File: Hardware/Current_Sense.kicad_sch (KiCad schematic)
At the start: 35 parts, among them IC2 INA241A4IDR, IC3 AMC1350DWVR, IC4 TLV9002QDRQ1, J6 Scrut Conn, SW3 Scrut Select, U9 REF35125QDBVR

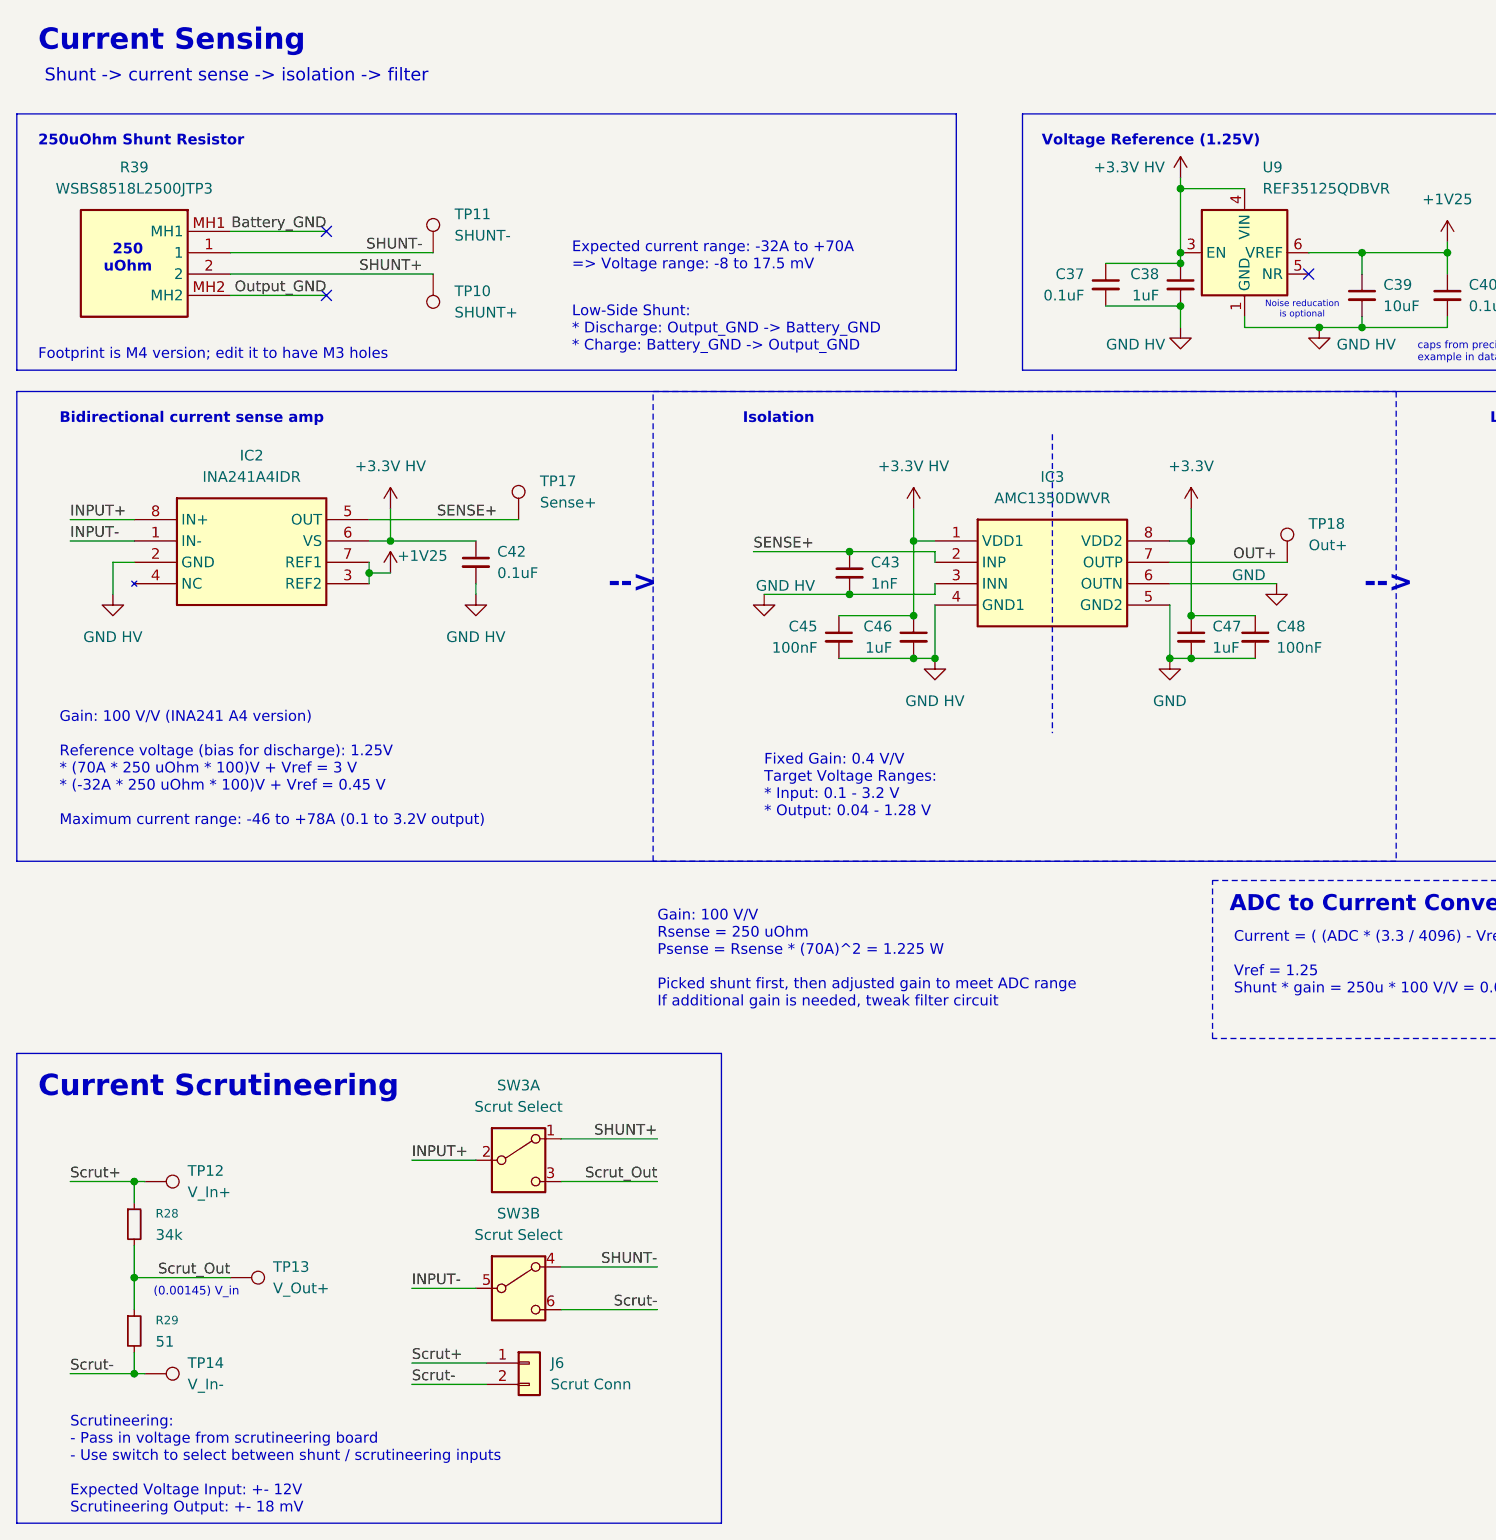
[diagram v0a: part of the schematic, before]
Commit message: added documentation for current range; added VBUS led
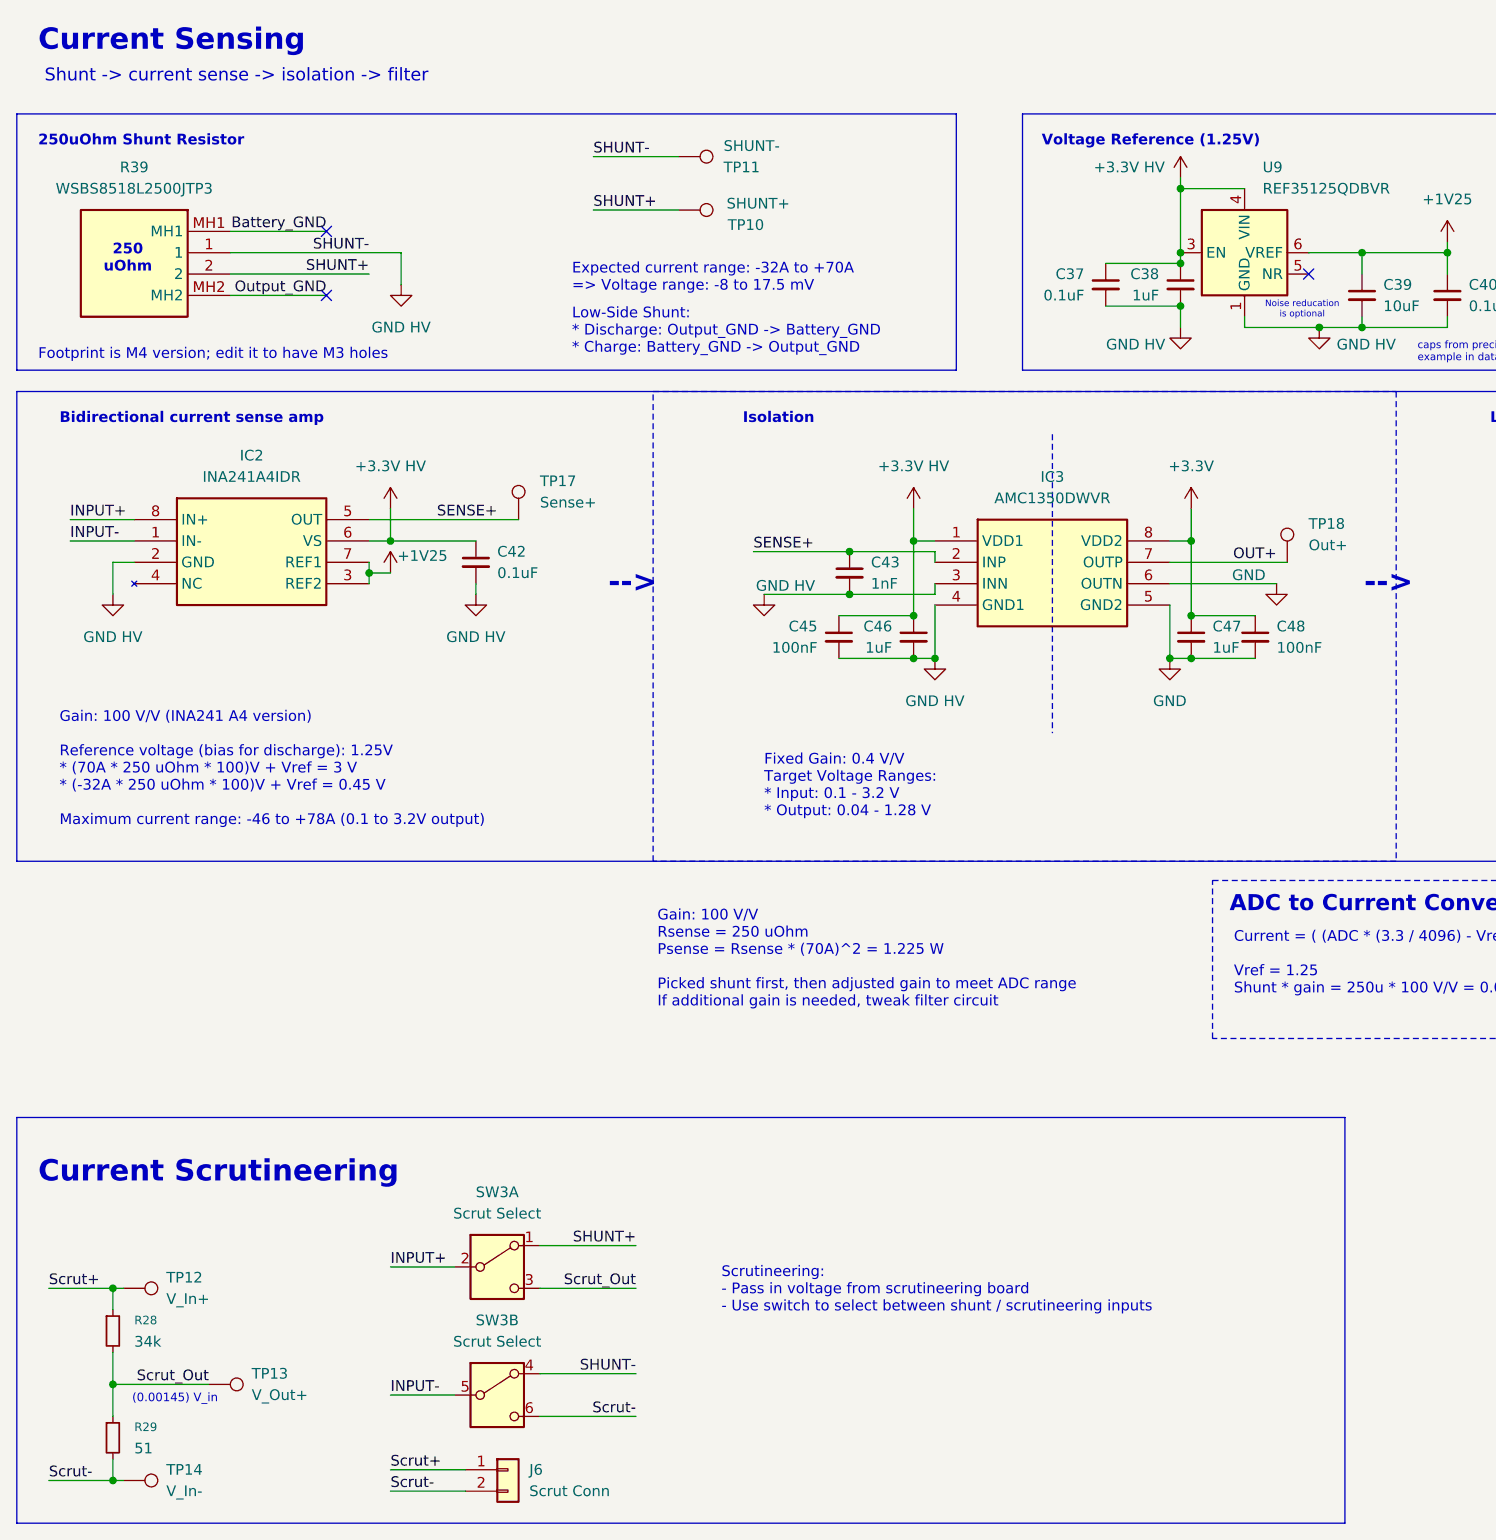
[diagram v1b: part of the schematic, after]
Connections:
- net SHUNT- is gone; now on net GND HV: R39.1, SW3.4 (A), TP11.1
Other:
- note added: "Scrutineering: - Pass in voltage from scrutineering board - Use switch to select between shunt / scrutineering inputs"
- note removed: "Scrutineering: - Pass in voltage from scrutineering board - Use switch to select between shunt / scrutineering inputs Expected Voltage Input: +- 12V Scrutineering Output: +- 18 mV"
- moved on the sheet: J6, R28, R29, SW3A, SW3B, TP10, TP11, TP12, TP13, TP14

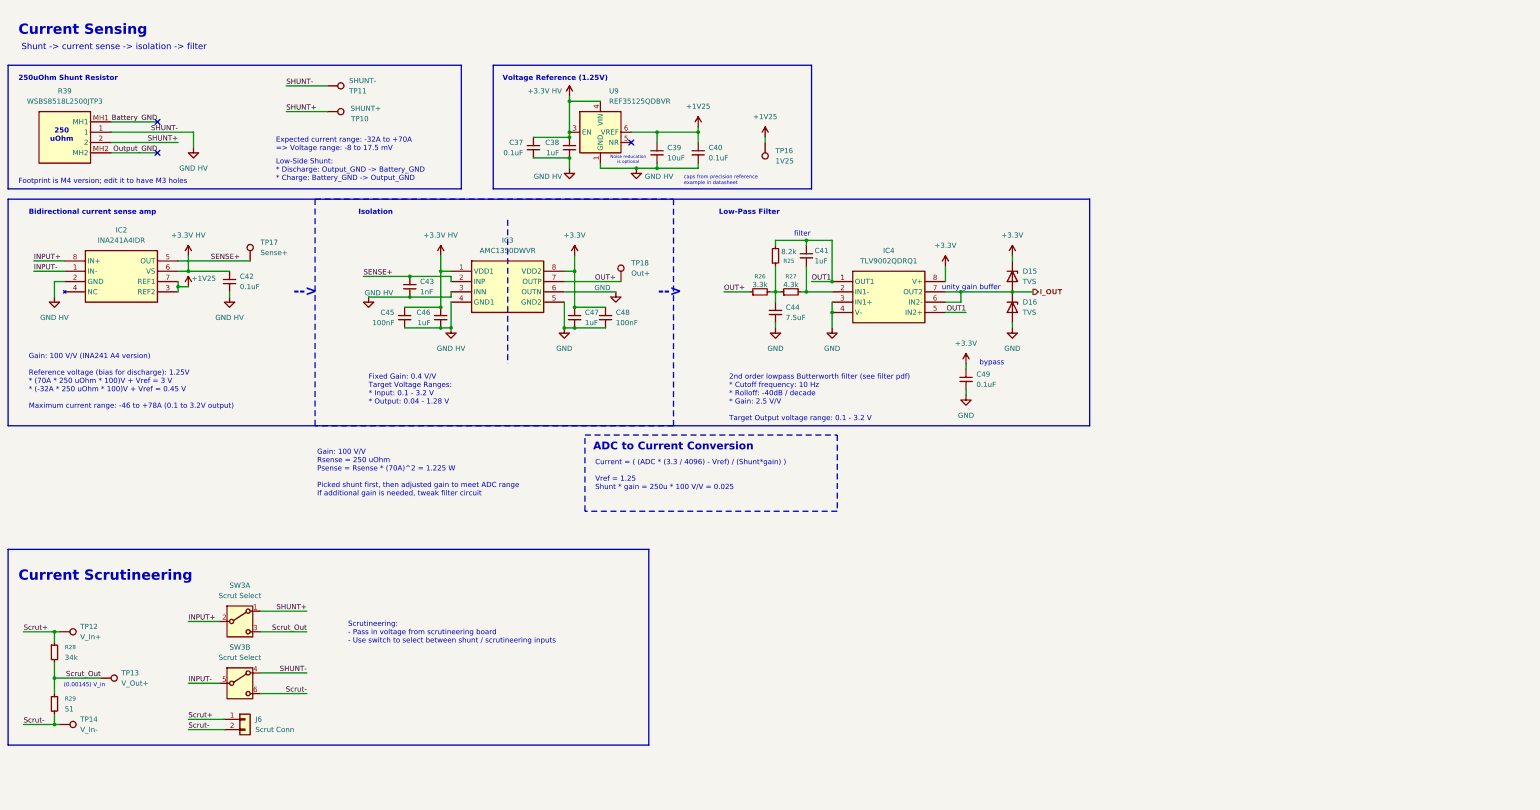
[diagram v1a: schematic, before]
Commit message: INA common-mode fixed (i think)
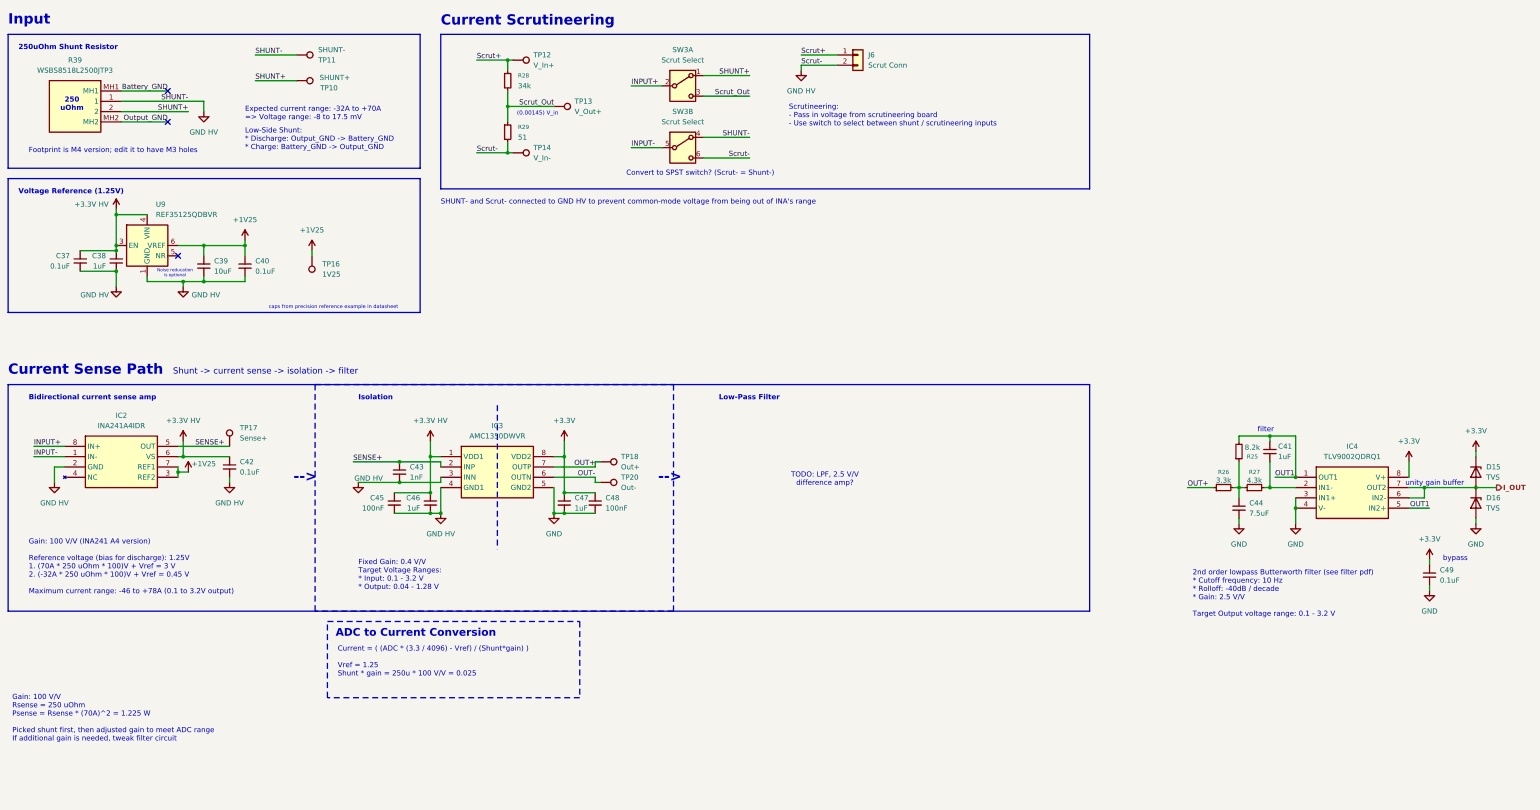
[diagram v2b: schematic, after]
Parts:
- added TP20: Out-, TestPoint:TestPoint_Keystone_5005-5009_Compact, symbol Connector:TestPoint
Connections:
- net Scrut- is gone; now on net GND HV: J6.2 (Pin_2), R29.2, SW3.6 (C), TP14.1
- net GND: no longer IC3.6 (OUTN)
- new net OUT-: IC3.6 (OUTN), TP20.1
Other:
- note added: "Convert to SPST switch? (Scrut- = Shunt-)"
- note added: "Current Sense Path"
- note added: "Gain: 100 V/V (INA241 A4 version) Reference voltage (bias for discharge): 1.25V 1. (70A * 250 uOhm * 100)V + Vref = 3 V 2. (-32A * 250 uOhm * 100)V + Vref = 0.45 V Maximum current range: -46 to +78A (0.1 to 3.2V output)"
- note added: "Input"
- note added: "SHUNT- and Scrut- connected to GND HV to prevent common-mode voltage from being out of INA's range"
- note added: "TODO: LPF, 2.5 V/V difference amp?"
- note removed: "Current Sensing"
- note removed: "Gain: 100 V/V (INA241 A4 version) Reference voltage (bias for discharge): 1.25V * (70A * 250 uOhm * 100)V + Vref = 3 V * (-32A * 250 uOhm * 100)V + Vref = 0.45 V Maximum current range: -46 to +78A (0.1 to 3.2V output)"
- moved on the sheet: C37, C38, C39, C40, C41, C42, C43, C44, C45, C46, C47, C48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

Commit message: differential amp for LPF
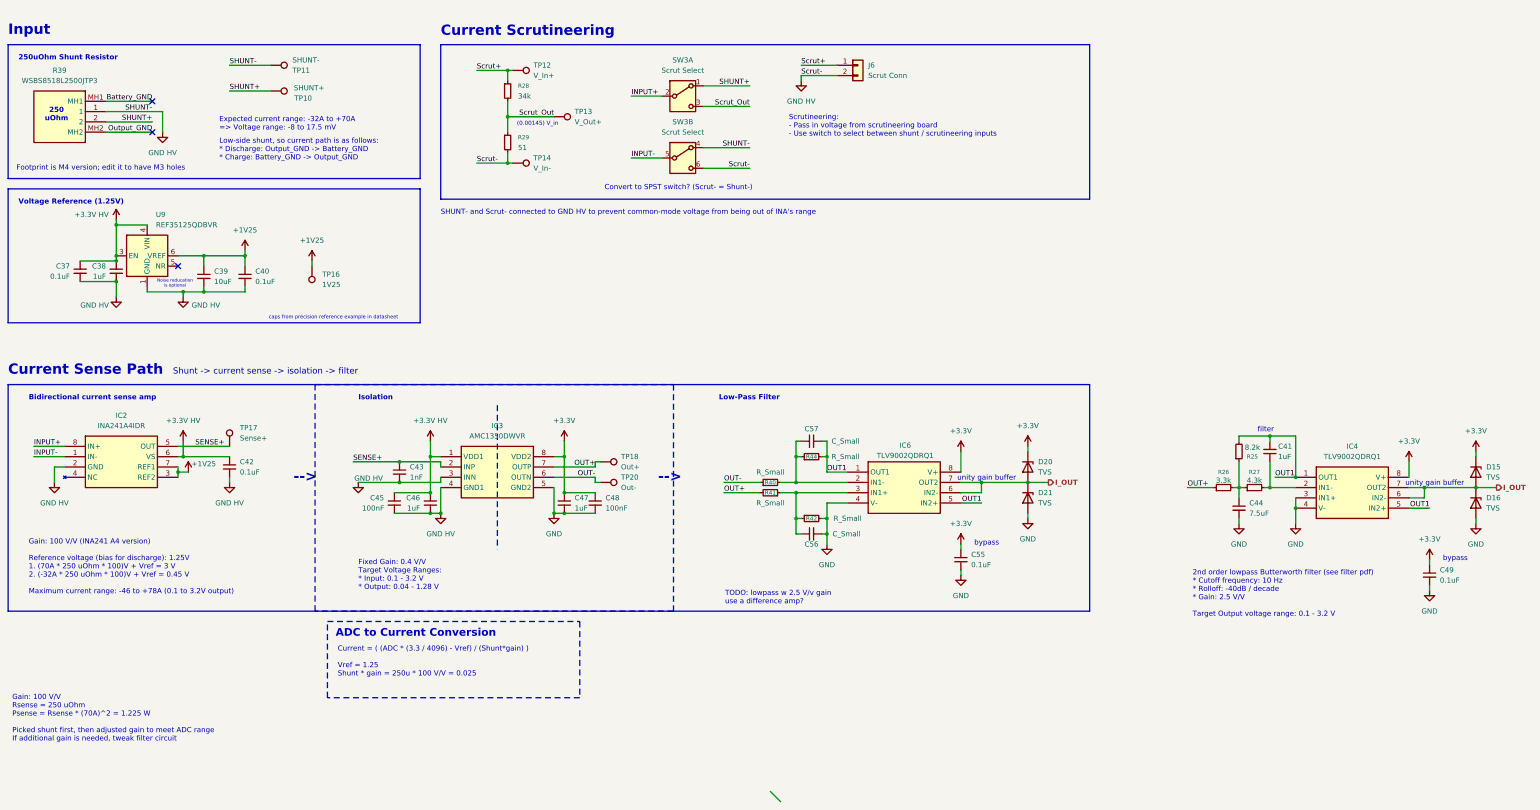
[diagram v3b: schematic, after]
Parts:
- added C55: 0.1uF, Capacitor_SMD:C_0603_1608Metric_Pad1.08x0.95mm_HandSolder, symbol Device:C_Small
- added C56, C57: C_Small, Capacitor_SMD:C_0603_1608Metric_Pad1.08x0.95mm_HandSolder, symbol Device:C_Small
- added D20, D21: TVS, Diode_SMD:D_SOD-123F, symbol Device:D_Zener
- added IC6: TLV9002QDRQ1, Parts:TLV9002QDRQ1, symbol TLV9002QDRQ1:TLV9002QDRQ1
- added R40, R41, R42, R44: R_Small, symbol Device:R_Small
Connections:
- net +3.3V: now also C55.1, D20.1 (K), IC6.8 (V+)
- net GND: now also C55.2, C56.2, D21.2 (A), IC6.4 (V-), R42.2
- net I_OUT: now also D20.2 (A), D21.1 (K), IC6.6 (IN2-), IC6.7 (OUT2)
- net OUT+: now also R41.2
- net OUT-: now also R40.1
- net OUT1: now also C57.2, IC6.1 (OUT1), IC6.5 (IN2+), R44.2
- new net: C57.1, IC6.2 (IN1-), R40.2, R44.1
- new net: C56.1, IC6.3 (IN1+), R41.1, R42.1
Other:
- note added: "Low-side shunt, so current path is as follows: * Discharge: Output_GND -> Battery_GND * Charge: Battery_GND -> Output_GND"
- note added: "TODO: lowpass w 2.5 V/v gain use a difference amp?"
- note removed: "Low-Side Shunt: * Discharge: Output_GND -> Battery_GND * Charge: Battery_GND -> Output_GND"
- note removed: "TODO: LPF, 2.5 V/V difference amp?"
- moved on the sheet: C37, C38, C39, C40, J6, R28, R29, R39, SW3A, SW3B, TP10, TP11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

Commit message: diff amp / LPF
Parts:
- removed C41: 1uF, Capacitor_SMD:C_0603_1608Metric_Pad1.08x0.95mm_HandSolder, symbol Device:C_Small
- removed C44: 7.5uF, Capacitor_SMD:C_0603_1608Metric_Pad1.08x0.95mm_HandSolder, symbol Device:C_Small
- removed C49: 0.1uF, Capacitor_SMD:C_0603_1608Metric_Pad1.08x0.95mm_HandSolder, symbol Device:C_Small
- removed D15, D16: TVS, Diode_SMD:D_SOD-123F, symbol Device:D_Zener
- removed IC4: TLV9002QDRQ1, Parts:TLV9002QDRQ1, symbol TLV9002QDRQ1:TLV9002QDRQ1
- removed R25: 8.2k, Resistor_SMD:R_0603_1608Metric_Pad0.98x0.95mm_HandSolder, symbol Device:R_Small
- removed R26: 3.3k, Resistor_SMD:R_0603_1608Metric_Pad0.98x0.95mm_HandSolder, symbol Device:R_Small
- removed R27: 4.3k, Resistor_SMD:R_0603_1608Metric_Pad0.98x0.95mm_HandSolder, symbol Device:R_Small
- C56, C57: value C_Small -> 330pF
- R40, R41: value R_Small -> 1.3k
- R42, R44: value R_Small -> 3.3k
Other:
- note added: "Differential Amplifier + Active LPF Vout = [(OUT+) - (OUT-)] * Gain * Gain: 2.54 V/V [gain = R2/R1 = 3.3k/1.3k] * 1st order lowpass [-20 db/dec] * Cutoff freq = 146 Hz [f = 1/(2*pi*R2*C)]"
- note removed: "2nd order lowpass Butterworth filter (see filter pdf) * Cutoff frequency: 10 Hz * Rolloff: -40dB / decade * Gain: 2.5 V/V Target Output voltage range: 0.1 - 3.2 V"
- note removed: "TODO: lowpass w 2.5 V/v gain use a difference amp?"
- note removed: "filter"
- moved on the sheet: C55, C56, C57, D20, D21, IC6, R40, R41, R42, R44
